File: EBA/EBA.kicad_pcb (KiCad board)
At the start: 2 copper layers, 6 parts, among them P1 CONN_01X03, P2 CONN_01X02

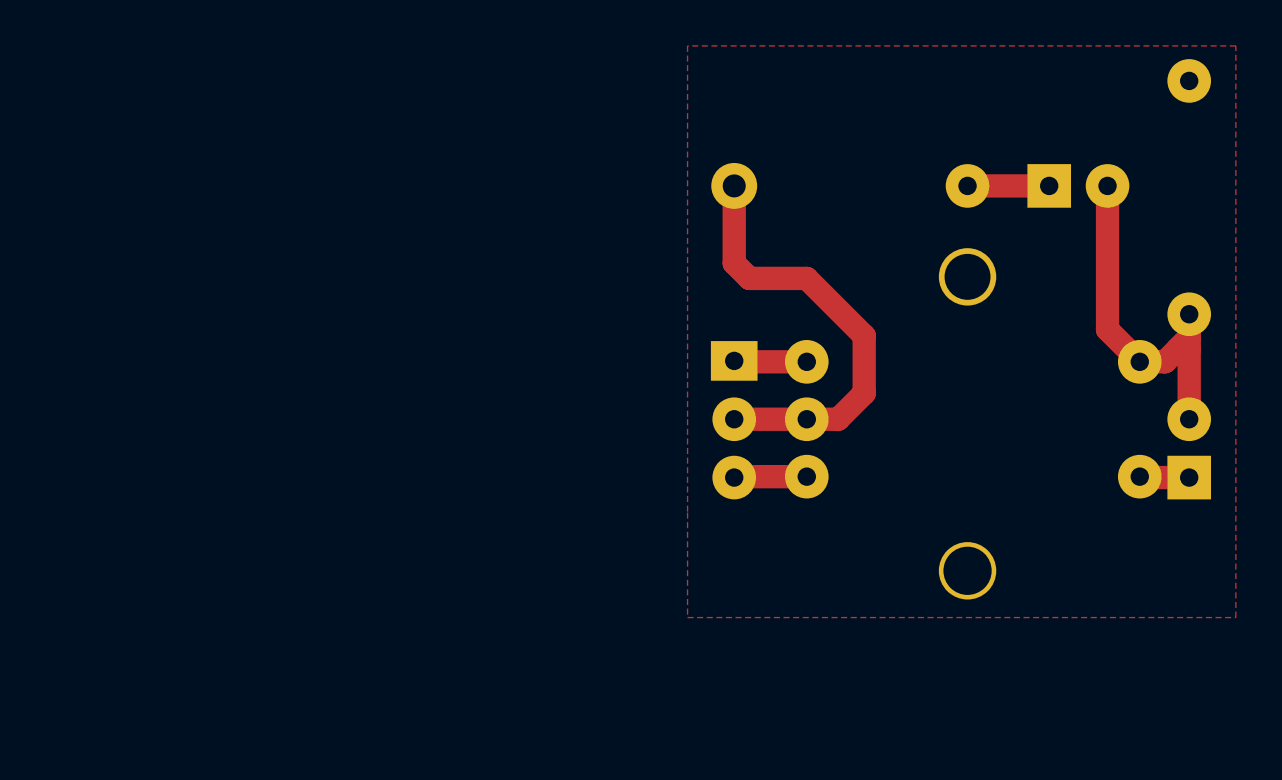
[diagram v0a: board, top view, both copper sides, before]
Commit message: Changed drill size of encoder pins to make it fit better
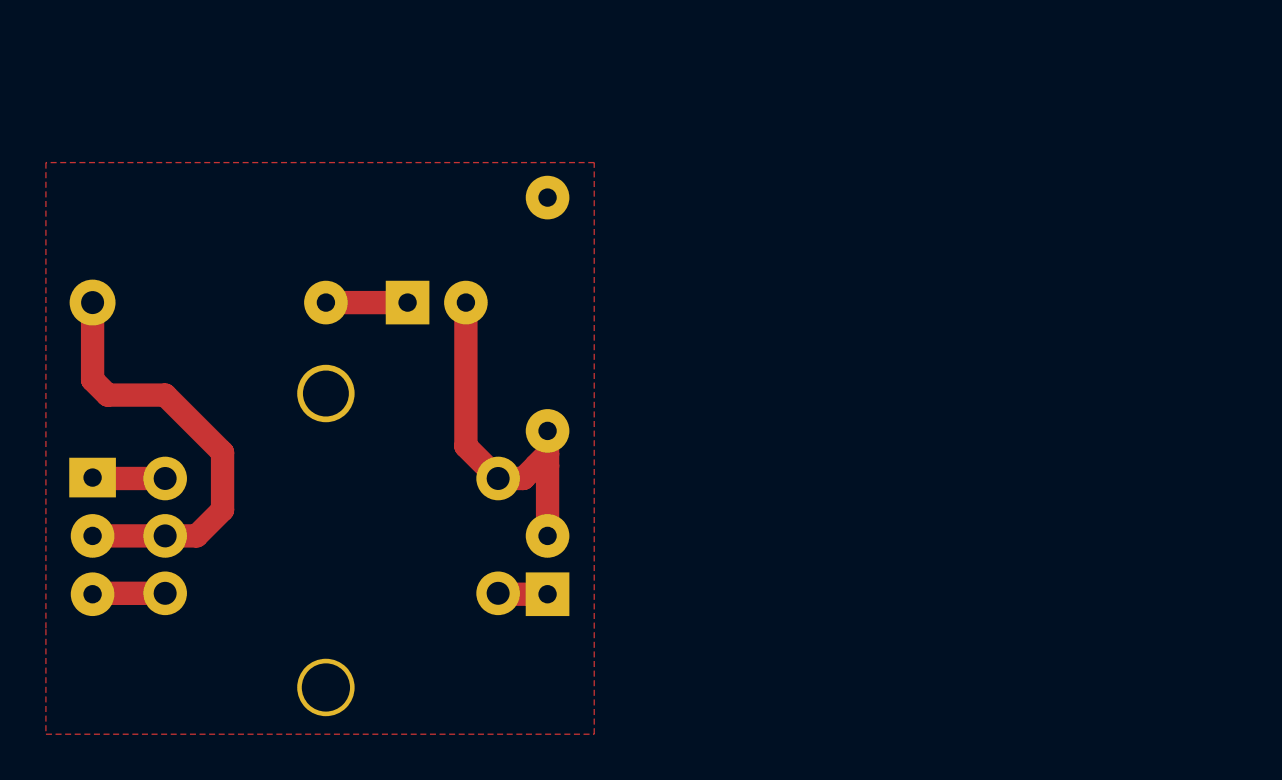
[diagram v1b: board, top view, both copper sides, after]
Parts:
- moved D1 28.4 mm to (102.6, 98.6)
- moved R1 28.4 mm to (94.0, 98.6)
- moved EN1 28.4 mm to (99.1, 108.7)
- moved P1 28.4 mm to (88.9, 106.2)
- moved P2 28.4 mm to (108.7, 111.3)
- moved R2 28.4 mm to (108.7, 99.1)
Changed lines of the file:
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@@
     (mod_text_width 0.15)
     (pad_size 1.9 1.9)
-    (pad_drill 0.8)
+    (pad_drill 1)
     (pad_to_mask_clearance 0)
     (aux_axis_origin 0 0)
@@
   )
   (module LEDs:LED-5MM (layer B.Cu)
-    (at 130.556 93.472)
+    (at 102.616 98.552)
     (descr "LED 5mm round vertical")
     (tags "LED 5mm round vertical")
@@
   )
   (module library:ENCODER_5_PINS (layer B.Cu)
-    (at 127 103.632)
+    (at 99.06 108.712)
     (fp_text reference EN1 (at -5.842 -9.144) (layer B.SilkS)
       (effects (font (size 1 1) (thickness 0.15)) (justify mirror))
@@
     (fp_line (start 1.778 6.604) (end 7.62 6.604) (layer B.SilkS) (width 0.15))
     (fp_line (start -6.858 6.604) (end -1.778 6.604) (layer B.SilkS) (width 0.15))
-    (pad 1 thru_hole circle (at -7 2.5) (size 1.9 1.9) (drill 0.8) (layers *.Cu *.Mask B.SilkS)
+    (pad 1 thru_hole circle (at -7 2.5) (size 1.9 1.9) (drill 1) (layers *.Cu *.Mask B.SilkS)
       (net 3 "Net-(EN1-Pad1)"))
-    (pad 2 thru_hole circle (at -7 0) (size 1.9 1.9) (drill 0.8) (layers *.Cu *.Mask B.SilkS)
-      (net 4 GND))
-    (pad 3 thru_hole circle (at -7 -2.5) (size 1.9 1.9) (drill 0.8) (layers *.Cu *.Mask B.SilkS)
+    (pad 2 thru_hole circle (at -7 0) (size 1.9 1.9) (drill 1) (layers *.Cu *.Mask B.SilkS)
+      (net 4 GND))
+    (pad 3 thru_hole circle (at -7 -2.5) (size 1.9 1.9) (drill 1) (layers *.Cu *.Mask B.SilkS)
       (net 5 "Net-(EN1-Pad3)"))
-    (pad 4 thru_hole circle (at 7.5 2.5) (size 1.9 1.9) (drill 0.8) (layers *.Cu *.Mask B.SilkS)
+    (pad 4 thru_hole circle (at 7.5 2.5) (size 1.9 1.9) (drill 1) (layers *.Cu *.Mask B.SilkS)
       (net 6 "Net-(EN1-Pad4)"))
-    (pad 5 thru_hole circle (at 7.5 -2.5) (size 1.9 1.9) (drill 0.8) (layers *.Cu *.Mask B.SilkS)
+    (pad 5 thru_hole circle (at 7.5 -2.5) (size 1.9 1.9) (drill 1) (layers *.Cu *.Mask B.SilkS)
       (net 2 "Net-(D1-Pad2)"))
     (pad "" np_thru_hole circle (at 0 6.6) (size 2.5 2.5) (drill 2.1) (layers *.Cu *.Mask B.SilkS))
@@
   )
   (module Pin_Headers:Pin_Header_Straight_1x03 (layer B.Cu)
-    (at 116.84 101.092 180)
+    (at 88.9 106.172 180)
     (descr "Through hole pin header")
     (tags "pin header")
@@
   )
   (module Pin_Headers:Pin_Header_Straight_1x02 (layer B.Cu)
-    (at 136.652 106.172)
+    (at 108.712 111.252)
     (descr "Through hole pin header")
     (tags "pin header")
@@
   )
   (module Resistors_ThroughHole:Resistor_Horizontal_RM10mm (layer B.Cu)
-    (at 121.92 93.472)
+    (at 93.98 98.552)
     (descr "Resistor, Axial,  RM 10mm, 1/3W,")
     (tags "Resistor, Axial, RM 10mm, 1/3W,")
@@
   )
   (module Resistors_ThroughHole:Resistor_Horizontal_RM10mm (layer B.Cu)
-    (at 136.652 93.98 270)
+    (at 108.712 99.06 270)
     (descr "Resistor, Axial,  RM 10mm, 1/3W,")
     (tags "Resistor, Axial, RM 10mm, 1/3W,")
@@
     )
   )
-  (segment (start 127 93.472) (end 130.556 93.472) (width 1.016) (layer F.Cu) (net 1) (status C00000))
-  (segment (start 133.096 93.472) (end 133.096 99.728) (width 1.016) (layer F.Cu) (net 2) (status 400000))
-  (segment (start 133.096 99.728) (end 134.5 101.132) (width 1.016) (layer F.Cu) (net 2) (status 800000))
-  (segment (start 134.5 101.132) (end 135.596 101.132) (width 1.016) (layer F.Cu) (net 2) (status 400000))
-  (segment (start 136.144 100.584) (end 136.652 100.584) (width 1.016) (layer F.Cu) (net 2))
-  (segment (start 136.652 100.076) (end 136.144 100.584) (width 1.016) (layer F.Cu) (net 2))
-  (segment (start 135.596 101.132) (end 136.652 100.076) (width 1.016) (layer F.Cu) (net 2))
-  (segment (start 136.652 103.632) (end 136.652 100.584) (width 1.016) (layer F.Cu) (net 2) (status 400000))
-  (segment (start 136.652 100.584) (end 136.652 99.06) (width 1.016) (layer F.Cu) (net 2) (status 800000))
-  (segment (start 120 106.132) (end 116.88 106.132) (width 1.016) (layer F.Cu) (net 3) (status C00000))
-  (segment (start 116.88 106.132) (end 116.84 106.172) (width 1.016) (layer F.Cu) (net 3) (status C00000))
-  (segment (start 120 103.632) (end 121.368 103.632) (width 1.016) (layer F.Cu) (net 4) (status 400000))
-  (segment (start 116.84 96.84) (end 116.84 93.472) (width 1.016) (layer F.Cu) (net 4) (status 800000))
-  (segment (start 117.5 97.5) (end 116.84 96.84) (width 1.016) (layer F.Cu) (net 4))
-  (segment (start 120 97.5) (end 117.5 97.5) (width 1.016) (layer F.Cu) (net 4))
-  (segment (start 122.5 100) (end 120 97.5) (width 1.016) (layer F.Cu) (net 4))
-  (segment (start 122.5 102.5) (end 122.5 100) (width 1.016) (layer F.Cu) (net 4))
-  (segment (start 121.368 103.632) (end 122.5 102.5) (width 1.016) (layer F.Cu) (net 4))
-  (segment (start 120 103.632) (end 116.84 103.632) (width 1.016) (layer F.Cu) (net 4) (status C00000))
-  (segment (start 120 101.132) (end 116.88 101.132) (width 1.016) (layer F.Cu) (net 5) (status C00000))
-  (segment (start 116.88 101.132) (end 116.84 101.092) (width 1.016) (layer F.Cu) (net 5) (status C00000))
-  (segment (start 136.652 106.172) (end 134.54 106.172) (width 1.016) (layer F.Cu) (net 6) (status C00000))
-  (segment (start 134.54 106.172) (end 134.5 106.132) (width 1.016) (layer F.Cu) (net 6) (status C00000))
+  (segment (start 99.06 98.552) (end 102.616 98.552) (width 1.016) (layer F.Cu) (net 1))
+  (segment (start 105.156 98.552) (end 105.156 104.808) (width 1.016) (layer F.Cu) (net 2))
+  (segment (start 105.156 104.808) (end 106.56 106.212) (width 1.016) (layer F.Cu) (net 2))
+  (segment (start 106.56 106.212) (end 107.656 106.212) (width 1.016) (layer F.Cu) (net 2))
+  (segment (start 108.204 105.664) (end 108.712 105.664) (width 1.016) (layer F.Cu) (net 2))
+  (segment (start 108.712 105.156) (end 108.204 105.664) (width 1.016) (layer F.Cu) (net 2))
+  (segment (start 107.656 106.212) (end 108.712 105.156) (width 1.016) (layer F.Cu) (net 2))
+  (segment (start 108.712 108.712) (end 108.712 105.664) (width 1.016) (layer F.Cu) (net 2))
+  (segment (start 108.712 105.664) (end 108.712 104.14) (width 1.016) (layer F.Cu) (net 2))
+  (segment (start 92.06 111.212) (end 88.94 111.212) (width 1.016) (layer F.Cu) (net 3))
+  (segment (start 88.94 111.212) (end 88.9 111.252) (width 1.016) (layer F.Cu) (net 3))
+  (segment (start 92.06 108.712) (end 93.428 108.712) (width 1.016) (layer F.Cu) (net 4))
+  (segment (start 88.9 101.92) (end 88.9 98.552) (width 1.016) (layer F.Cu) (net 4))
+  (segment (start 89.56 102.58) (end 88.9 101.92) (width 1.016) (layer F.Cu) (net 4))
+  (segment (start 92.06 102.58) (end 89.56 102.58) (width 1.016) (layer F.Cu) (net 4))
+  (segment (start 94.56 105.08) (end 92.06 102.58) (width 1.016) (layer F.Cu) (net 4))
+  (segment (start 94.56 107.58) (end 94.56 105.08) (width 1.016) (layer F.Cu) (net 4))
+  (segment (start 93.428 108.712) (end 94.56 107.58) (width 1.016) (layer F.Cu) (net 4))
+  (segment (start 92.06 108.712) (end 88.9 108.712) (width 1.016) (layer F.Cu) (net 4))
+  (segment (start 92.06 106.212) (end 88.94 106.212) (width 1.016) (layer F.Cu) (net 5))
+  (segment (start 88.94 106.212) (end 88.9 106.172) (width 1.016) (layer F.Cu) (net 5))
+  (segment (start 108.712 111.252) (end 106.6 111.252) (width 1.016) (layer F.Cu) (net 6))
+  (segment (start 106.6 111.252) (end 106.56 111.212) (width 1.016) (layer F.Cu) (net 6))
   (zone (net 4) (net_name GND) (layer F.Cu) (hatch edge 0.508)
     (connect_pads (clearance 0.508))
@@
     (polygon
       (pts
-        (xy 114.808 107.696) (xy 114.808 112.268) (xy 138.684 112.268) (xy 138.684 87.376) (xy 114.808 87.376)
-        (xy 114.808 103.632)
+        (xy 86.868 112.776) (xy 86.868 117.348) (xy 110.744 117.348) (xy 110.744 92.456) (xy 86.868 92.456)
+        (xy 86.868 108.712)
       )
     )
